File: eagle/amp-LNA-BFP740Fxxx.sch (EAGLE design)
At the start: 23 parts, among them J1 142-0701-851, J2 142-0701-851, Q1 PMOS, Q2 BFP740F

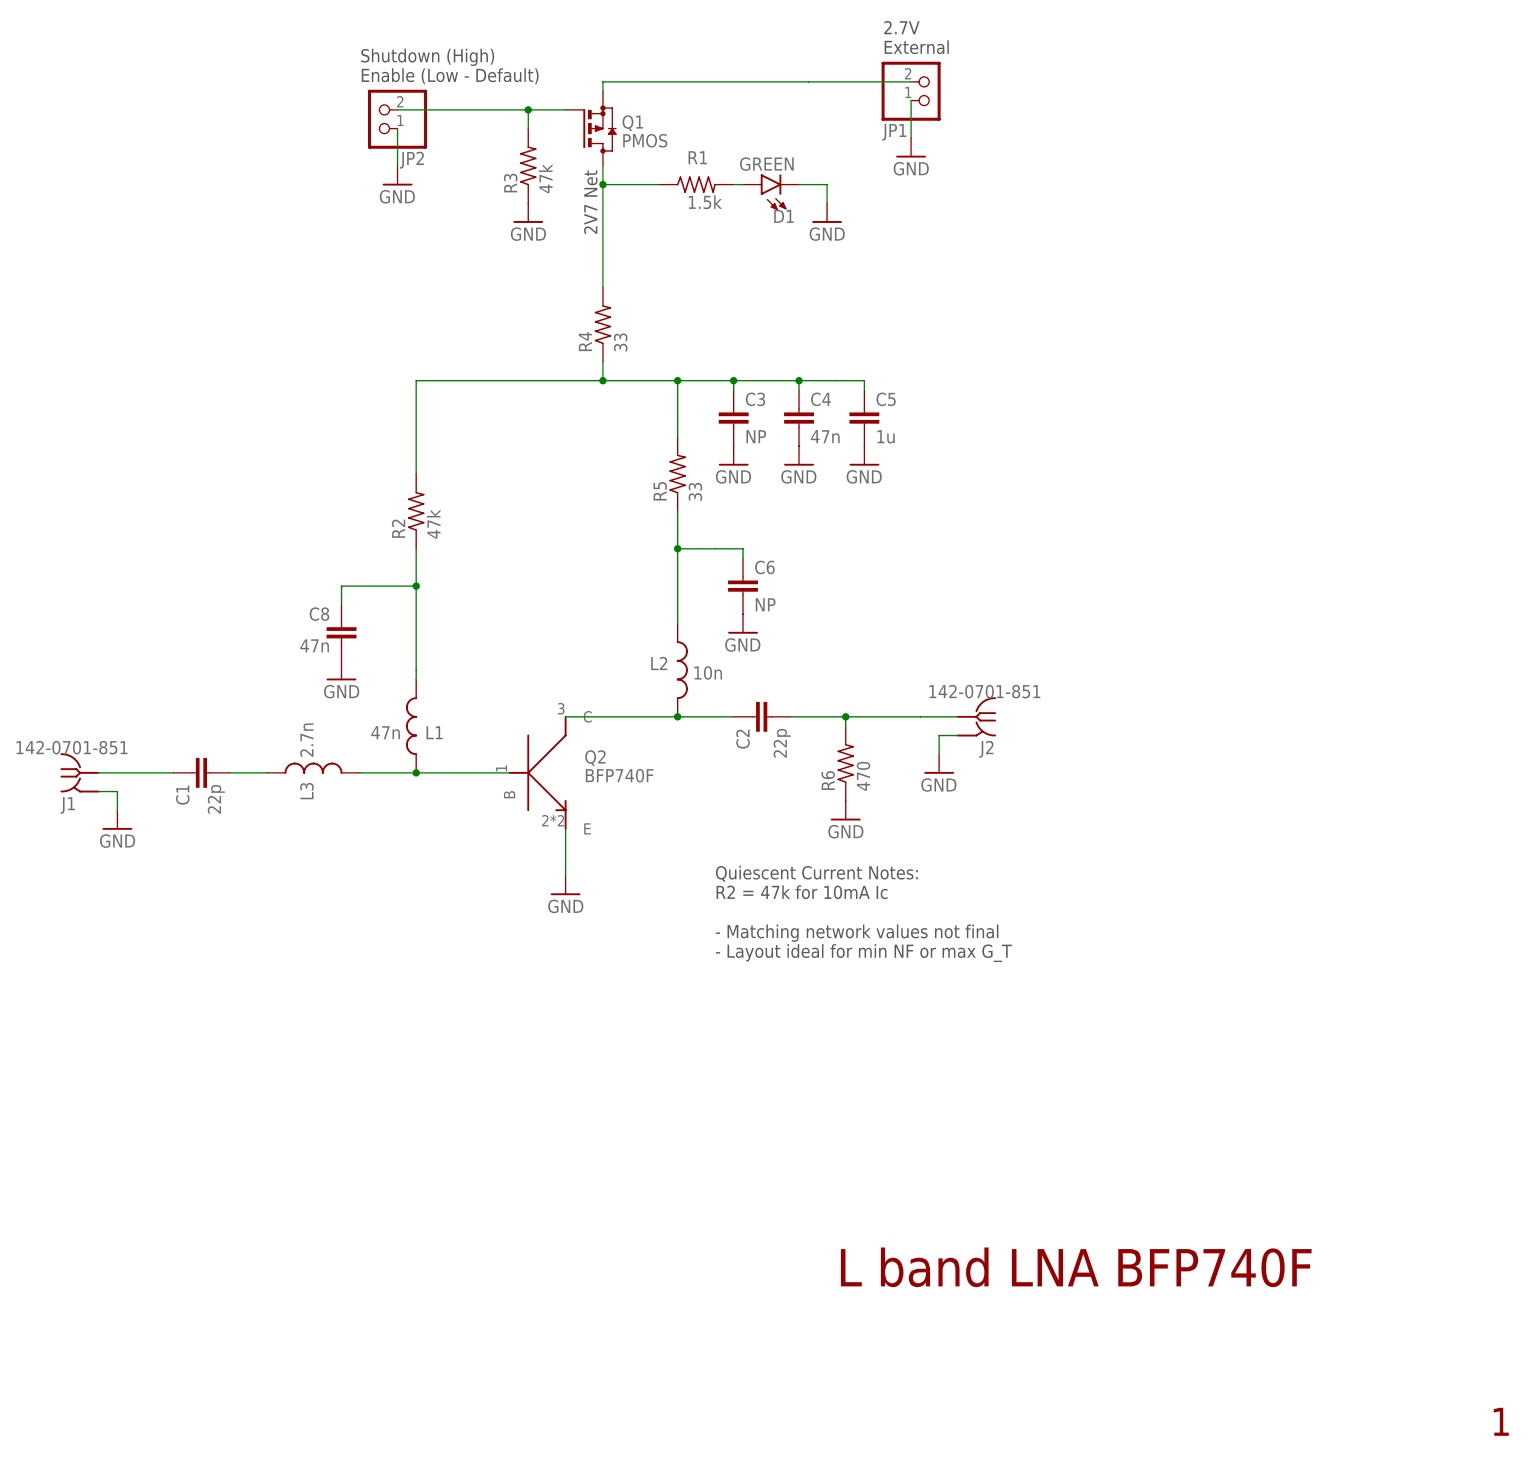
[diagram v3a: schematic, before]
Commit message: Update LNA-BFP740F values
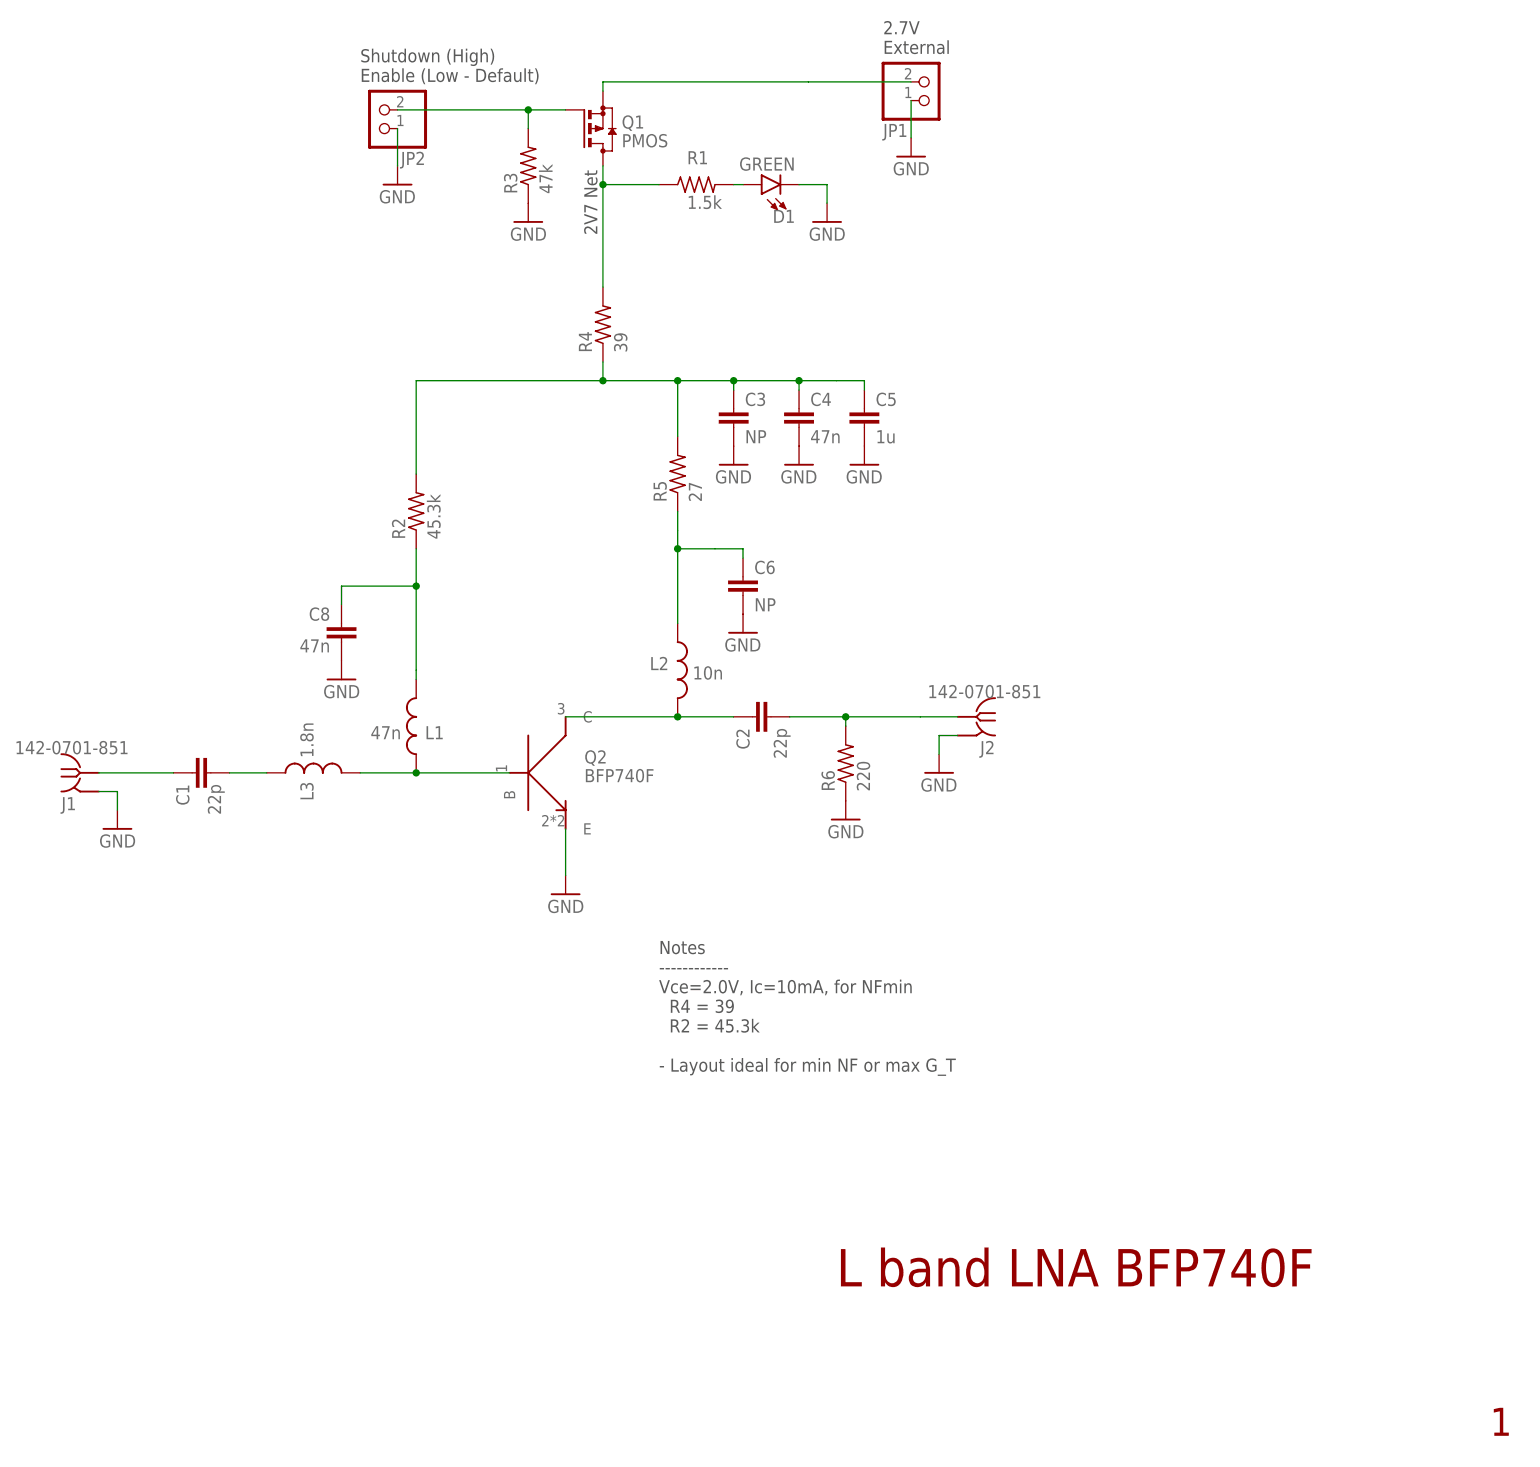
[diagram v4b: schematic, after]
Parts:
- L3: value 2.7n -> 1.8n
- R2: value 47k -> 45.3k
- R4: value 33 -> 39
- R5: value 33 -> 27
- R6: value 470 -> 220
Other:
- note added: "Notes ------------ Vce=2.0V, Ic=10mA, for NFmin R4 = 39 R2 = 45.3k - Layout ideal for min NF or max G_T"
- note removed: "Quiescent Current Notes: R2 = 47k for 10mA Ic - Matching network values not final - Layout ideal for min NF or max G_T"
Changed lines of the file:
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@@
 <?xml version="1.0" encoding="utf-8"?>
 <!DOCTYPE eagle SYSTEM "eagle.dtd">
-<eagle version="9.2.2">
+<eagle version="9.5.1">
 <drawing>
 <settings>
@@
 <part name="R3" library="oresat-rcl" deviceset="R-US_" device="0402-B-NOSILK" value="47k"/>
 <part name="GND3" library="supply1" library_urn="urn:adsk.eagle:library:371" deviceset="GND" device=""/>
-<part name="R5" library="oresat-rcl" deviceset="R-US_" device="0603-C-NOSILK" value="33"/>
+<part name="R5" library="oresat-rcl" deviceset="R-US_" device="0603-C-NOSILK" value="27"/>
 <part name="GND2" library="supply1" library_urn="urn:adsk.eagle:library:371" deviceset="GND" device=""/>
 <part name="Q2" library="Q-Infineon-BFPXXX-RF-BJT" deviceset="BFPXXXF" device="" value="BFP740F"/>
 <part name="C6" library="oresat-rcl" deviceset="C-EU" device="0402-B-NOSILK" value="NP"/>
 <part name="GND6" library="supply1" library_urn="urn:adsk.eagle:library:371" deviceset="GND" device=""/>
-<part name="R2" library="oresat-rcl" deviceset="R-US_" device="0603-C-NOSILK" value="47k"/>
-<part name="L3" library="oresat-rcl" deviceset="L-US" device="0402-C-NOSILK" value="2.7n"/>
-<part name="R4" library="oresat-rcl" deviceset="R-US_" device="0603-C-NOSILK" value="33"/>
+<part name="R2" library="oresat-rcl" deviceset="R-US_" device="0603-C-NOSILK" value="45.3k"/>
+<part name="L3" library="oresat-rcl" deviceset="L-US" device="0402-C-NOSILK" value="1.8n"/>
+<part name="R4" library="oresat-rcl" deviceset="R-US_" device="0603-C-NOSILK" value="39"/>
 <part name="L2" library="oresat-rcl" deviceset="L-US" device="0603-C-NOSILK" value="10n"/>
 <part name="GND9" library="supply1" library_urn="urn:adsk.eagle:library:371" deviceset="GND" device=""/>
-<part name="R6" library="oresat-rcl" deviceset="R-US_" device="0603-C-NOSILK" value="470"/>
+<part name="R6" library="oresat-rcl" deviceset="R-US_" device="0603-C-NOSILK" value="220"/>
 </parts>
 <sheets>
@@
 Enable (Low - Default)</text>
 <text x="144.018" y="169.672" size="1.778" layer="97" rot="R90">2V7 Net</text>
-<text x="160.02" y="83.82" size="1.778" layer="97" align="top-left">Quiescent Current Notes:
-R2 = 47k for 10mA Ic
-- Matching network values not final
+<text x="152.4" y="73.66" size="1.778" layer="97" align="top-left">Notes
+------------
+Vce=2.0V, Ic=10mA, for NFmin
+  R4 = 39
+  R2 = 45.3k
 - Layout ideal for min NF or max G_T</text>
 </plain>
